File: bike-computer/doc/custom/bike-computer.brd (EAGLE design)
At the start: 100 x 80 mm, 12 parts, among them Q1 2N3820, Q2 2N3820, Q3 2N3820, X1 5566-8

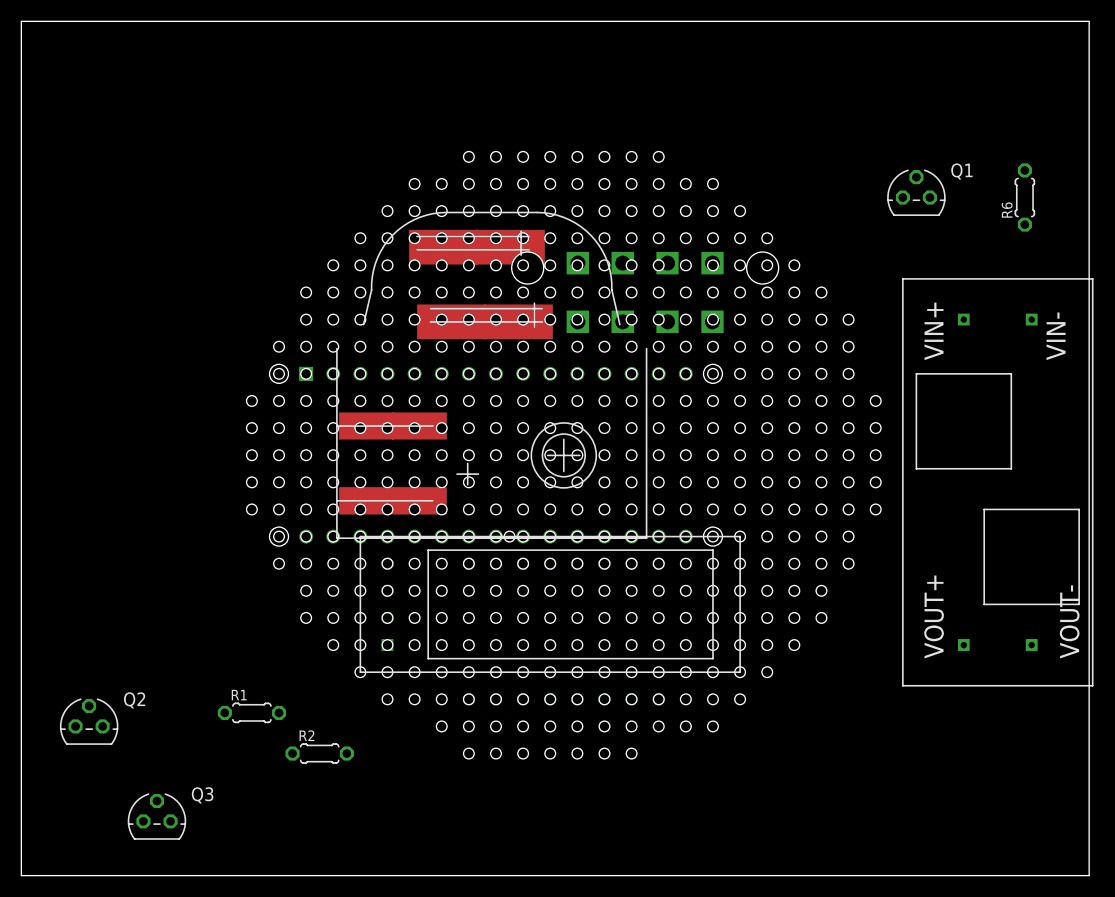
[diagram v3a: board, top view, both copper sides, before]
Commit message: Change from Arduino Nano to Arduino Pro Mini.
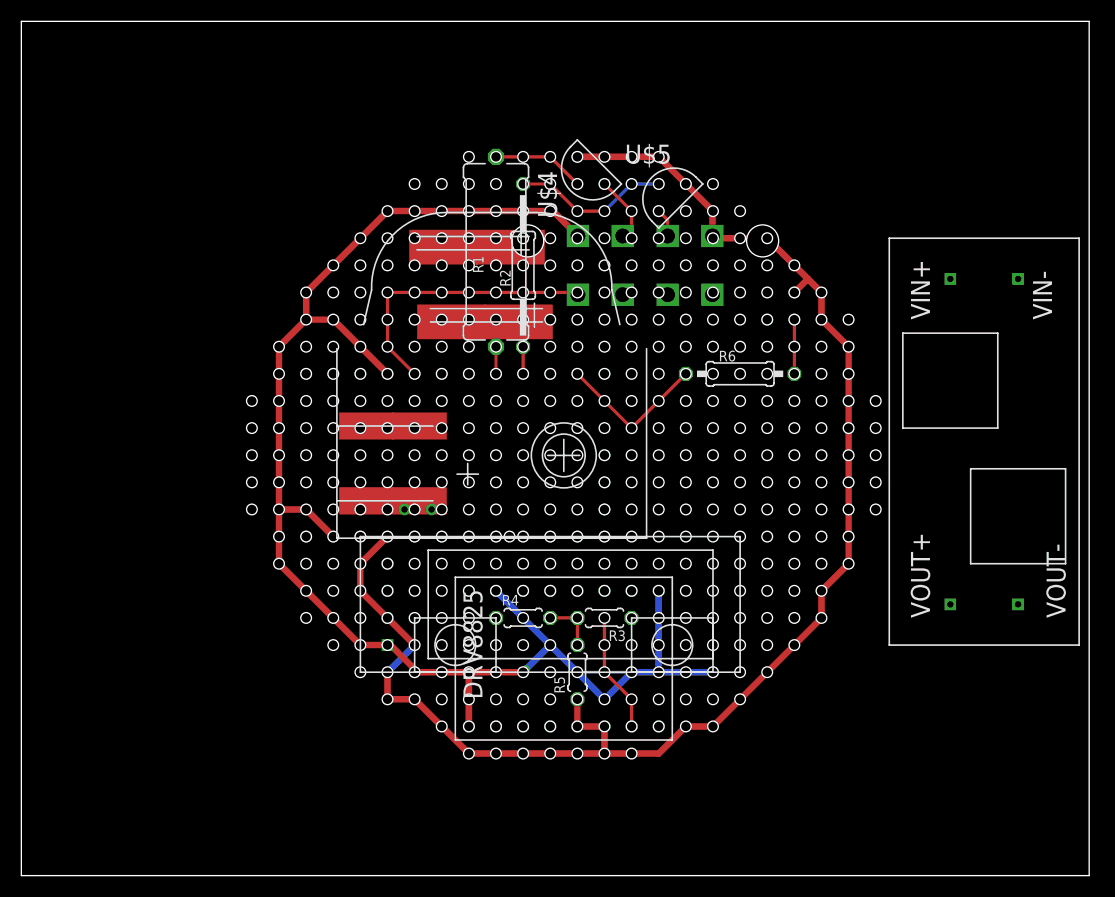
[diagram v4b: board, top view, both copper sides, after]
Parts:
- removed ARDUINO_NANO1: (no value), ArduinoNanoV30:ARDUINO_NANO
- removed Q1, Q2, Q3: 2N3820, transistor-small-signal:TO92F
- added R3, R4, R5: (no value), rcl:0204/5
- added U$4, U$5, U$6: BS250, bike_computer:TO92(2.54)
- added U$7: (no value), bike_computer:ARDUINO_PRO_MINI
- added U$8, U$9: MICRO_SWITCH, bike_computer:MICRO_SWITCH
- R1: device rcl:0204/5 -> rcl:0617/17
- R2: device rcl:0204/5 -> rcl:0207/15
- R6: device rcl:0204/5 -> rcl:0207/10
- moved R2 49.5 mm to (47.0, 57.1), turned to 90 degrees
- moved R1 48.9 mm to (44.5, 58.4), turned to 90 degrees
- moved R6 31.4 mm to (67.3, 47.0), turned to 0 degrees
- moved U$2 4.02 mm to (90.2, 40.6)
- moved DRV8825 2.54 mm to (50.8, 20.3), flipped to the top
- moved X1 2.54 mm to (58.4, 57.1)
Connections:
- removed net GND: ARDUINO_NANO1.19
- removed net VIN: ARDUINO_NANO1.15
- new net KEYS_INPUT: R3.2, R4.2, R5.2, U$7.A1
- new net N$10: R3.1, U$8.1, U$8.2
- new net N$11: R4.1, U$9.1, U$9.2
- net +5V: now also R5.1, U$4.S, U$5.S, U$6.S, U$7.VCC, X1.8; no longer ARDUINO_NANO1.12, Q1.S, Q2.S, Q3.S, X1.2
- net 0V: now also U$7.GND@1, U$7.GND@2, U$8.3, U$8.4, U$9.3, U$9.4, X1.5; no longer ARDUINO_NANO1.14, X1.1
- net 12V_ENABLE: now also U$7.D8; no longer ARDUINO_NANO1.23
- net BACK_LIGHT_PWM: now also U$7.D6; no longer ARDUINO_NANO1.26
- net BACK_LIGHT_VOLTAGE: now also U$5.D, X1.7; no longer Q3.D, X1.3
- net DIR: now also U$7.D13; no longer ARDUINO_NANO1.21
- net FRONT_LIGHT_PWM: now also U$7.D5; no longer ARDUINO_NANO1.25
- net FRONT_LIGHT_VOLTAGE: now also U$4.D; no longer Q2.D
- net N$5: now also U$4.G; no longer Q2.G
- net N$6: now also U$6.G; no longer Q1.G
- net N$7: now also U$6.D; no longer Q1.D
- net N$8: now also U$5.G; no longer Q3.G
- net SCL: now also U$7.A5; no longer ARDUINO_NANO1.9
- net SDA: now also U$7.A4; no longer ARDUINO_NANO1.8
- net SPEED_INPUT: now also U$7.D2, X1.1; no longer ARDUINO_NANO1.24, X1.5
- net STEP: now also U$7.A0; no longer ARDUINO_NANO1.20
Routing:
- net 0V: track 0.00 -> 146.3 mm, vias 0 -> 1
- net +5V: track 0.00 -> 139.0 mm, vias 0 -> 3
- net SPEED_INPUT: track 0.00 -> 26.6 mm
- net N$8: track 0.00 -> 14.8 mm, vias 0 -> 1
- net 12V_ENABLE: track 0.00 -> 14.4 mm
- net STEP: track 0.00 -> 11.2 mm
- net N$5: track 0.00 -> 8.67 mm
- net FRONT_LIGHT_VOLTAGE: track 0.00 -> 6.27 mm
- net N$6: track 0.00 -> 5.08 mm
- net KEYS_INPUT: track 0.00 -> 5.08 mm
- net BACK_LIGHT_VOLTAGE: track 0.00 -> 2.67 mm
- net FRONT_LIGHT_PWM: track 0.00 -> 2.54 mm
- net BACK_LIGHT_PWM: track 0.00 -> 2.54 mm

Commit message: [Bike] Further work on schematics.
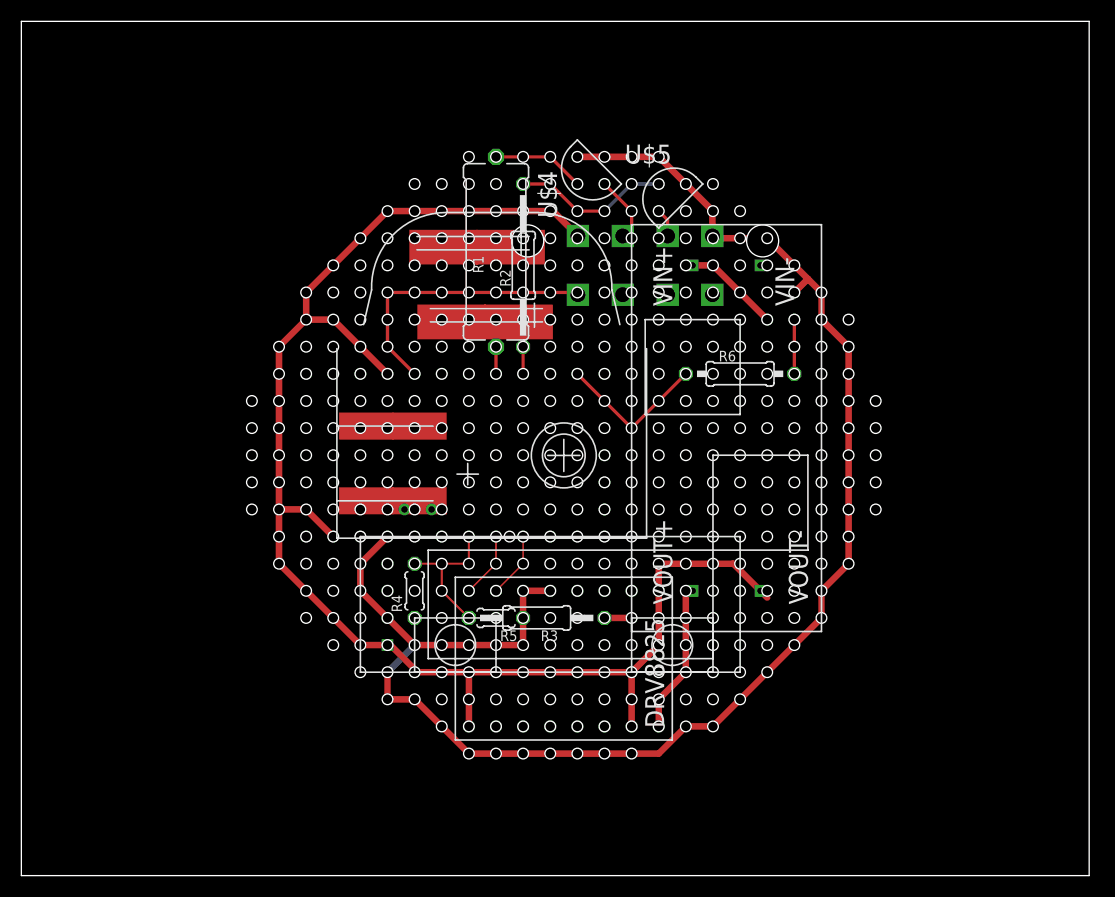
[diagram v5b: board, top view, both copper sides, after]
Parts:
- R3: device rcl:0204/5 -> rcl:0207/12
- moved U$2 24.2 mm to (66.0, 41.9)
- moved R4 10.5 mm to (36.8, 26.7), turned to 90 degrees
- moved R5 9.16 mm to (44.5, 24.1), turned to 180 degrees
- moved R3 6.35 mm to (48.3, 24.1)
- turned DRV8825 to 270 degrees
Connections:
- net 0V: no longer U$8.4
- net DIR: now also U$7.A0; no longer U$7.D13
- net N$10: no longer U$8.2
- net STEP: now also U$7.D13; no longer U$7.A0
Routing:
- net +12V: track 0.00 -> 15.0 mm
- net +5V: track 139.0 -> 149.2 mm, vias 3 -> 2
- net N$7: track 0.00 -> 9.09 mm
- net KEYS_INPUT: track 5.08 -> 13.8 mm
- net DIR: track 0.00 -> 6.13 mm
- net STEP: track 11.2 -> 6.13 mm
- net 0V: track 146.3 -> 142.1 mm, vias 1 -> 0
- net N$10: track 0.00 -> 2.54 mm

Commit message: [Bike] More work on schematics.
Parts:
- R6: device rcl:0207/10 -> rcl:0207/15
- moved R6 3.59 mm to (64.8, 49.5)
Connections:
- net +12V: now also DRV8825.VMOT; no longer DRV8825.P$9
- net +5V: now also DRV8825.RESET, DRV8825.SLEEP; no longer DRV8825.P$5, DRV8825.P$6
- net 0V: now also DRV8825.ENABLE, DRV8825.GNDLOGIC, DRV8825.GNDMOT; no longer DRV8825.P$1, DRV8825.P$10, DRV8825.P$16
- net DIR: now also DRV8825.DIR; no longer DRV8825.P$8
- net N$1: now also DRV8825.B2; no longer DRV8825.P$11
- net N$2: now also DRV8825.B1; no longer DRV8825.P$12
- net N$3: now also DRV8825.A1; no longer DRV8825.P$13
- net N$4: now also DRV8825.A2; no longer DRV8825.P$14
- net STEP: now also DRV8825.STEP; no longer DRV8825.P$7
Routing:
- net +5V: track 149.2 -> 117.9 mm, vias 2 -> 1
- net 12V_ENABLE: track 14.4 -> 7.62 mm
- net N$6: track 5.08 -> 2.54 mm
- net 0V: track 142.1 -> 143.6 mm
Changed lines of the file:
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@@
 <attribute name="VALUE" x="49.3014" y="55.0164" size="0.9906" layer="27" ratio="10" rot="R90"/>
 </element>
-<element name="R6" library="rcl" library_urn="urn:adsk.eagle:library:334" package="0207/10" package3d_urn="urn:adsk.eagle:package:23491/2" value="" x="67.31" y="46.99" smashed="yes">
-<attribute name="NAME" x="65.3034" y="48.1584" size="0.9906" layer="25" ratio="10"/>
-<attribute name="POPULARITY" value="81" x="67.31" y="46.99" size="1.778" layer="27" display="off"/>
-<attribute name="SPICEPREFIX" value="R" x="67.31" y="46.99" size="1.778" layer="27" display="off"/>
-<attribute name="VALUE" x="65.1764" y="44.6786" size="0.9906" layer="27" ratio="10"/>
+<element name="R6" library="rcl" library_urn="urn:adsk.eagle:library:334" package="0207/15" package3d_urn="urn:adsk.eagle:package:23492/1" value="" x="64.77" y="49.53" smashed="yes">
+<attribute name="NAME" x="62.7634" y="50.6984" size="0.9906" layer="25" ratio="10"/>
+<attribute name="POPULARITY" value="2" x="64.77" y="49.53" size="1.778" layer="27" display="off"/>
+<attribute name="SPICEPREFIX" value="R" x="64.77" y="49.53" size="1.778" layer="27" display="off"/>
+<attribute name="VALUE" x="62.6364" y="47.2186" size="0.9906" layer="27" ratio="10"/>
 </element>
 <element name="R3" library="rcl" library_urn="urn:adsk.eagle:library:334" package="0207/12" package3d_urn="urn:adsk.eagle:package:23489/1" value="" x="48.26" y="24.13" smashed="yes" rot="R180">
@@
 <contactref element="U$1" pad="P$5"/>
 <contactref element="U$1" pad="P$6"/>
-<contactref element="DRV8825" pad="P$11"/>
+<contactref element="DRV8825" pad="B2"/>
 <wire x1="39.55" y1="58.85" x2="45.8" y2="58.85" width="0" layer="19" extent="1-1"/>
-<wire x1="54.61" y1="13.97" x2="39.55" y2="58.85" width="0" layer="19" extent="1-1"/>
+<wire x1="54.61" y1="13.97" x2="45.8" y2="58.85" width="0" layer="19" extent="1-1"/>
 </signal>
 <signal name="N$2">
 <contactref element="U$1" pad="P$7"/>
 <contactref element="U$1" pad="P$8"/>
-<contactref element="DRV8825" pad="P$12"/>
+<contactref element="DRV8825" pad="B1"/>
 <wire x1="40.3" y1="51.85" x2="46.55" y2="51.85" width="0" layer="19" extent="1-1"/>
-<wire x1="52.07" y1="13.97" x2="40.3" y2="51.85" width="0" layer="19" extent="1-1"/>
+<wire x1="52.07" y1="13.97" x2="46.55" y2="51.85" width="0" layer="19" extent="1-1"/>
 </signal>
 <signal name="N$3">
 <contactref element="U$1" pad="P$1"/>
 <contactref element="U$1" pad="P$2"/>
-<contactref element="DRV8825" pad="P$13"/>
+<contactref element="DRV8825" pad="A1"/>
 <wire x1="32.3" y1="42.1" x2="37.3" y2="42.1" width="0" layer="19" extent="1-1"/>
-<wire x1="49.53" y1="13.97" x2="32.3" y2="42.1" width="0" layer="19" extent="1-1"/>
+<wire x1="49.53" y1="13.97" x2="37.3" y2="42.1" width="0" layer="19" extent="1-1"/>
 </signal>
 <signal name="N$4">
 <contactref element="U$1" pad="P$3"/>
 <contactref element="U$1" pad="P$4"/>
-<contactref element="DRV8825" pad="P$14"/>
+<contactref element="DRV8825" pad="A2"/>
 <wire x1="32.3" y1="35.1" x2="37.3" y2="35.1" width="0" layer="19" extent="1-1"/>
-<wire x1="46.99" y1="13.97" x2="32.3" y2="35.1" width="0" layer="19" extent="1-1"/>
+<wire x1="46.99" y1="13.97" x2="37.3" y2="35.1" width="0" layer="19" extent="1-1"/>
 </signal>
 <signal name="0V">
 <contactref element="U$3" pad="GND"/>
-<contactref element="DRV8825" pad="P$10"/>
-<contactref element="DRV8825" pad="P$16"/>
-<contactref element="DRV8825" pad="P$1"/>
+<contactref element="DRV8825" pad="GNDMOT"/>
+<contactref element="DRV8825" pad="GNDLOGIC"/>
+<contactref element="DRV8825" pad="ENABLE"/>
 <contactref element="U$2" pad="VIN-"/>
 <contactref element="U$2" pad="VOUT-"/>
@@
 <wire x1="29.21" y1="31.75" x2="26.67" y2="34.29" width="0.6096" layer="1"/>
 <wire x1="26.67" y1="34.29" x2="24.13" y2="34.29" width="0.6096" layer="1"/>
-<wire x1="34.29" y1="46.99" x2="29.21" y2="52.07" width="0.6096" layer="1"/>
-<wire x1="29.21" y1="52.07" x2="26.67" y2="52.07" width="0.6096" layer="1"/>
+<wire x1="26.67" y1="52.07" x2="29.21" y2="52.07" width="0.6096" layer="1"/>
 <contactref element="U$9" pad="3"/>
 <contactref element="U$9" pad="4"/>
@@
 <wire x1="57.15" y1="19.05" x2="59.69" y2="21.59" width="0.6096" layer="1"/>
 <wire x1="57.15" y1="19.05" x2="57.15" y2="13.97" width="0.6096" layer="1"/>
+<wire x1="29.21" y1="52.07" x2="31.75" y2="52.07" width="0.6096" layer="1"/>
+<wire x1="31.75" y1="52.07" x2="34.29" y2="49.53" width="0.6096" layer="1"/>
+<wire x1="34.29" y1="49.53" x2="34.29" y2="46.99" width="0.6096" layer="1"/>
 <wire x1="52.12" y1="59.9" x2="69.215" y2="57.15" width="0" layer="19" extent="1-1"/>
 <wire x1="36.83" y1="19.05" x2="36.5506" y2="19.3294" width="0" layer="19" extent="1-1"/>
@@
 <signal name="+5V">
 <contactref element="U$3" pad="VCC"/>
-<contactref element="DRV8825" pad="P$5"/>
-<contactref element="DRV8825" pad="P$6"/>
+<contactref element="DRV8825" pad="RESET"/>
+<contactref element="DRV8825" pad="SLEEP"/>
 <contactref element="R5" pad="1"/>
 <contactref element="U$4" pad="S"/>
@@
 <wire x1="74.93" y1="54.61" x2="74.93" y2="52.07" width="0.6096" layer="1"/>
 <wire x1="74.93" y1="52.07" x2="77.47" y2="49.53" width="0.6096" layer="1"/>
-<wire x1="77.47" y1="49.53" x2="77.47" y2="29.21" width="0.6096" layer="1"/>
-<wire x1="77.47" y1="29.21" x2="74.93" y2="26.67" width="0.6096" layer="1"/>
-<wire x1="74.93" y1="26.67" x2="74.93" y2="24.13" width="0.6096" layer="1"/>
-<wire x1="64.77" y1="13.97" x2="62.23" y2="13.97" width="0.6096" layer="1"/>
-<wire x1="62.23" y1="13.97" x2="59.69" y2="11.43" width="0.6096" layer="1"/>
-<wire x1="74.93" y1="24.13" x2="64.77" y2="13.97" width="0.6096" layer="1"/>
 <wire x1="72.39" y1="54.61" x2="73.66" y2="55.88" width="0.6096" layer="1"/>
 <contactref element="U$7" pad="VCC"/>
@@
 <wire x1="31.75" y1="26.67" x2="31.75" y2="29.21" width="0.6096" layer="1"/>
 <wire x1="31.75" y1="29.21" x2="34.29" y2="31.75" width="0.6096" layer="1"/>
-<wire x1="59.69" y1="11.43" x2="41.91" y2="11.43" width="0.6096" layer="1"/>
-<wire x1="41.91" y1="11.43" x2="36.83" y2="16.51" width="0.6096" layer="1"/>
-<wire x1="36.83" y1="16.51" x2="34.29" y2="16.51" width="0.6096" layer="1"/>
-<wire x1="34.29" y1="16.51" x2="34.29" y2="19.05" width="0.6096" layer="1"/>
-<via x="34.29" y="19.05" extent="1-16" drill="0.35"/>
-<wire x1="34.29" y1="19.05" x2="36.83" y2="21.59" width="0.6096" layer="16"/>
 <via x="36.83" y="21.59" extent="1-16" drill="0.35"/>
 <wire x1="36.83" y1="21.59" x2="46.99" y2="21.59" width="0.6096" layer="1"/>
@@
 <wire x1="46.99" y1="24.13" x2="46.99" y2="26.67" width="0.6096" layer="1"/>
 <wire x1="46.99" y1="26.67" x2="49.53" y2="26.67" width="0.6096" layer="1"/>
+<wire x1="77.47" y1="49.53" x2="77.47" y2="31.75" width="0.6096" layer="1"/>
+<wire x1="77.47" y1="31.75" x2="57.15" y2="31.75" width="0.6096" layer="1"/>
+<wire x1="57.15" y1="31.75" x2="57.15" y2="29.21" width="0.6096" layer="1"/>
+<wire x1="57.15" y1="29.21" x2="52.07" y2="29.21" width="0.6096" layer="1"/>
+<wire x1="52.07" y1="29.21" x2="49.53" y2="26.67" width="0.6096" layer="1"/>
 </signal>
 <signal name="STEP">
-<contactref element="DRV8825" pad="P$7"/>
+<contactref element="DRV8825" pad="STEP"/>
 <contactref element="U$7" pad="D13"/>
 <wire x1="44.45" y1="26.67" x2="46.99" y2="29.21" width="0.1524" layer="1"/>
@@
 </signal>
 <signal name="DIR">
-<contactref element="DRV8825" pad="P$8"/>
+<contactref element="DRV8825" pad="DIR"/>
 <contactref element="U$7" pad="A0"/>
 <wire x1="41.91" y1="26.67" x2="44.45" y2="29.21" width="0.1524" layer="1"/>
@@
 </signal>
 <signal name="+12V">
-<contactref element="DRV8825" pad="P$9"/>
+<contactref element="DRV8825" pad="VMOT"/>
 <contactref element="U$2" pad="VOUT+"/>
 <wire x1="62.23" y1="26.67" x2="62.865" y2="26.67" width="0.6096" layer="16"/>
@@
 <contactref element="R6" pad="1"/>
 <contactref element="U$7" pad="D8"/>
-<wire x1="52.07" y1="46.99" x2="57.15" y2="41.91" width="0.3048" layer="1"/>
-<wire x1="62.23" y1="46.99" x2="57.15" y2="41.91" width="0.3048" layer="1"/>
+<wire x1="52.07" y1="46.99" x2="52.07" y2="49.53" width="0.6096" layer="1"/>
+<wire x1="52.07" y1="49.53" x2="57.15" y2="49.53" width="0.6096" layer="1"/>
 </signal>
 <signal name="SPEED_INPUT">
@@
 <wire x1="52.12" y1="54.4" x2="51.91" y2="54.61" width="0.6096" layer="1"/>
 <wire x1="51.91" y1="54.61" x2="34.29" y2="54.61" width="0.3048" layer="1"/>
-<wire x1="34.29" y1="54.61" x2="34.29" y2="49.53" width="0.3048" layer="1"/>
-<wire x1="34.29" y1="49.53" x2="36.83" y2="46.99" width="0.3048" layer="1"/>
+<wire x1="34.29" y1="54.61" x2="34.29" y2="52.07" width="0.1524" layer="1"/>
+<wire x1="34.29" y1="52.07" x2="36.83" y2="49.53" width="0.1524" layer="1"/>
+<wire x1="36.83" y1="49.53" x2="36.83" y2="46.99" width="0.1524" layer="1"/>
 </signal>
 <signal name="FRONT_LIGHT_PWM">
@@
 <contactref element="R6" pad="2"/>
 <contactref element="U$6" pad="G"/>
-<wire x1="72.39" y1="46.99" x2="72.39" y2="52.07" width="0.3048" layer="1"/>
+<wire x1="72.39" y1="49.53" x2="72.39" y2="52.07" width="0.6096" layer="1"/>
 </signal>
 <signal name="N$7">
